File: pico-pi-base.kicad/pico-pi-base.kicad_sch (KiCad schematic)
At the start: 10 parts, among them J1 GPIO, J2 JST-PH2 Bat Ext, J3 Grove, J4 JST-PH2 Bat Int, J5 Conn_SPI1, SW1 SW_Push, U1 Pico_nodbg

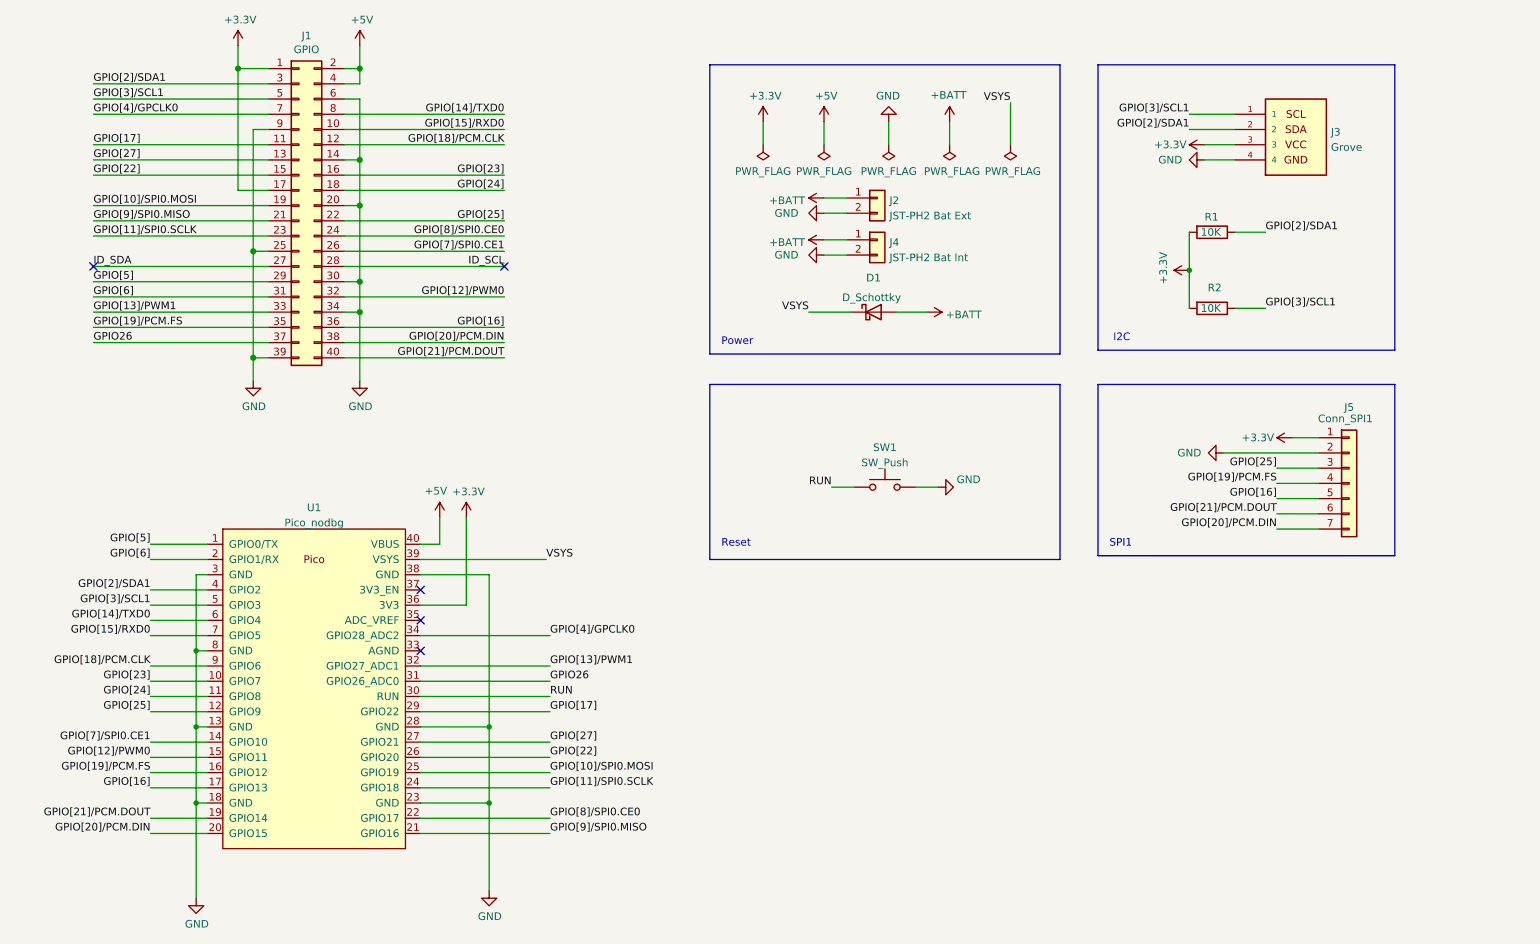
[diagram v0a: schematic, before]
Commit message: pico-pi-base Rev 1.2
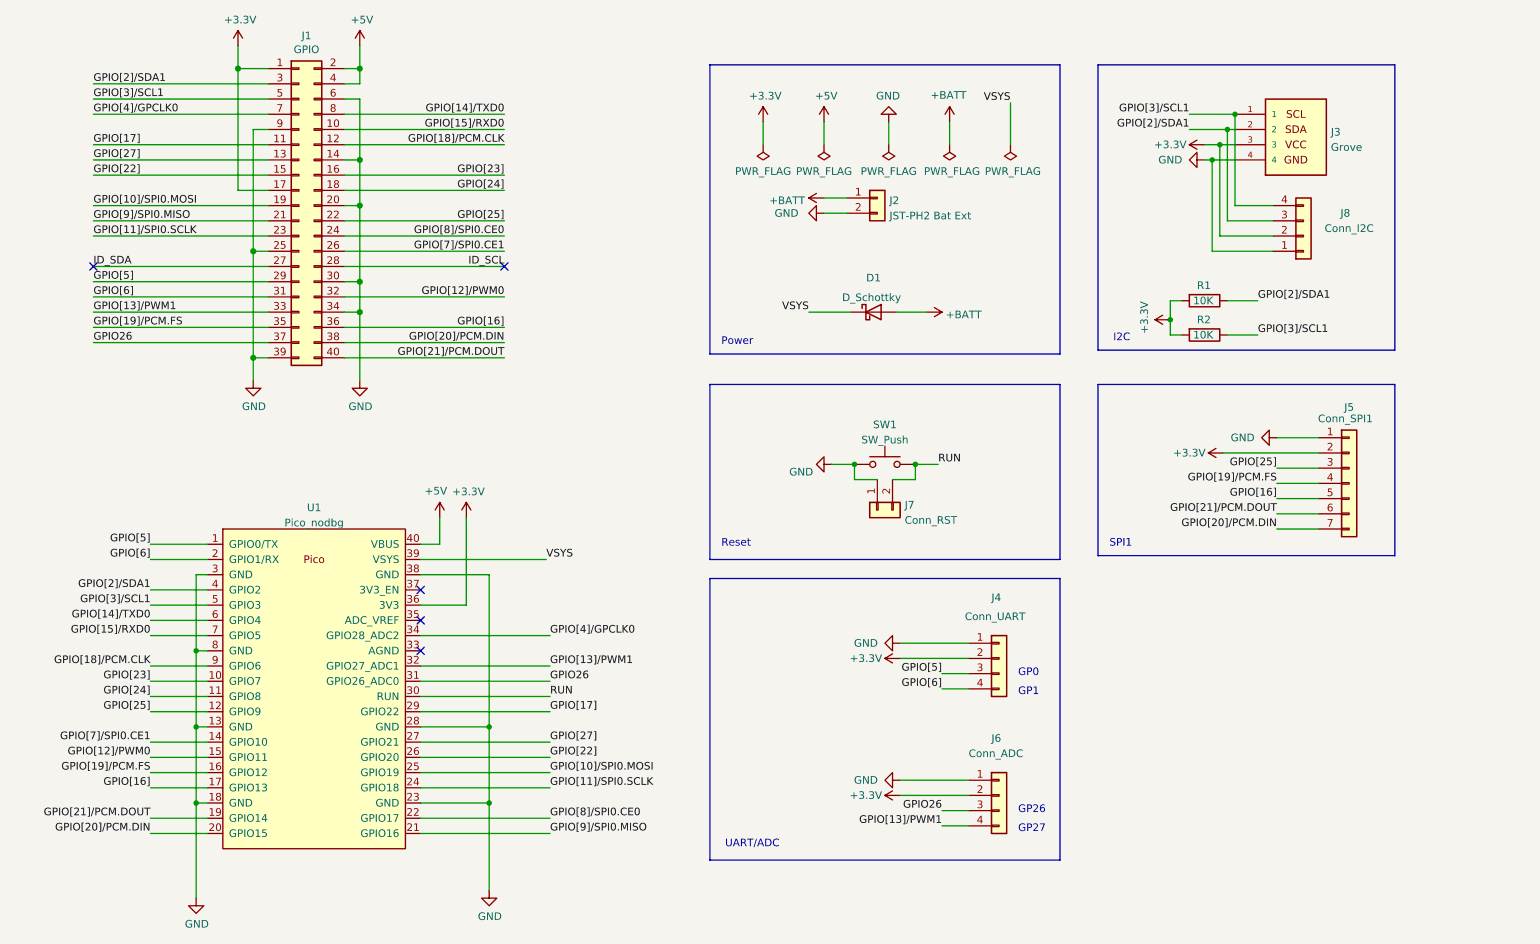
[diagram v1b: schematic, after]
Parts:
- removed J4: JST-PH2 Bat Int, Connector_JST:JST_PH_S2B-PH-SM4-TB_1x02-1MP_P2.00mm_Horizontal, symbol Connector_Generic:Conn_01x02
- added J4: Conn_UART, Connector_PinSocket_2.54mm:PinSocket_1x04_P2.54mm_Horizontal, symbol Connector_Generic:Conn_01x04
- added J6: Conn_ADC, Connector_PinSocket_2.54mm:PinSocket_1x04_P2.54mm_Horizontal, symbol Connector_Generic:Conn_01x04
- added J7: Conn_RST, Connector_PinHeader_2.54mm:PinHeader_1x02_P2.54mm_Horizontal, symbol Connector_Generic:Conn_01x02
- added J8: Conn_I2C, Connector_PinHeader_2.54mm:PinHeader_1x04_P2.54mm_Horizontal, symbol Connector_Generic:Conn_01x04
- J1: footprint Connector_PinSocket_2.54mm:PinSocket_2x20_P2.54mm_Vertical -> Connector_PinHeader_2.54mm:PinHeader_2x20_P2.54mm_Vertical
- R1, R2: LCSC C25744 -> C25804
- SW1: footprint Button_Switch_SMD:SW_SPST_B3U-3000P -> user:Microtaster_Horizontal
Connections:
- net +3.3V: now also J5.2 (Pin_2), J4.2 (Pin_2), J6.2 (Pin_2), J8.2 (Pin_2); no longer J5.1 (Pin_1)
- net GND: now also J5.1 (Pin_1), SW1.1, J4.1 (Pin_1), J6.1 (Pin_1), J7.1 (Pin_1), J8.1 (Pin_1); no longer J5.2 (Pin_2), SW1.2
- net GPIO26: now also J6.3 (Pin_3)
- net GPIO[13]/PWM1: now also J6.4 (Pin_4)
- net GPIO[2]/SDA1: now also J8.3 (Pin_3)
- net GPIO[3]/SCL1: now also J8.4 (Pin_4)
- net GPIO[5]: now also J4.3 (Pin_3)
- net GPIO[6]: now also J4.4 (Pin_4)
- net RUN: now also SW1.2, J7.2 (Pin_2); no longer SW1.1
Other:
- note added: "GP0"
- note added: "GP1"
- note added: "GP26"
- note added: "GP27"
- note added: "UART/ADC"
- moved on the sheet: R1, R2, SW1

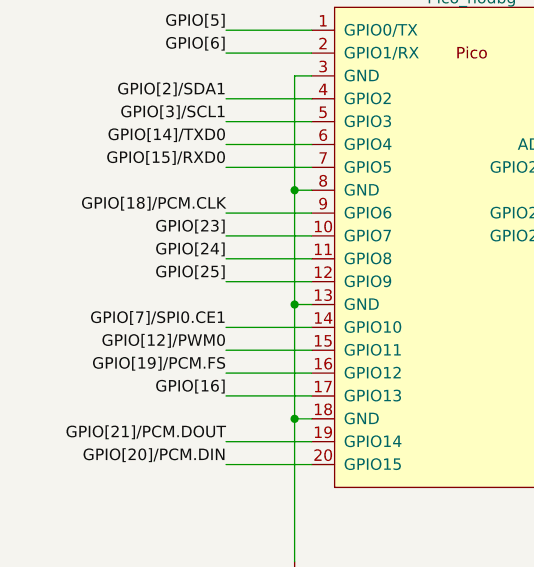
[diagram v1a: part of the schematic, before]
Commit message: Rev 2.0: swapped pins to support I2S
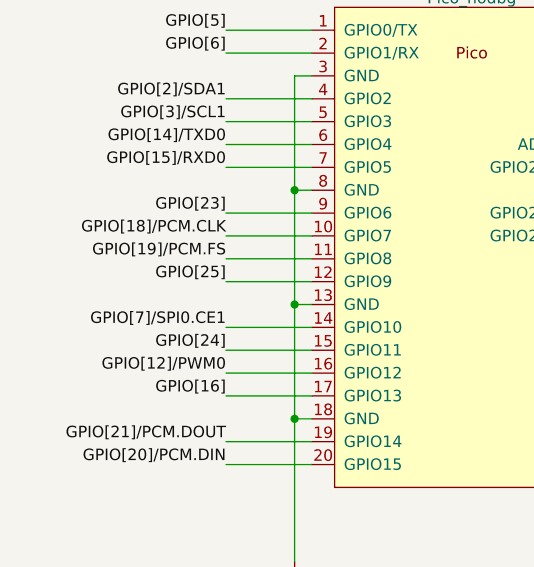
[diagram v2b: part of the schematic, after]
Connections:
- net GPIO[12]/PWM0: now also U1.16 (GPIO12); no longer U1.15 (GPIO11)
- net GPIO[18]/PCM.CLK: now also U1.10 (GPIO7); no longer U1.9 (GPIO6)
- net GPIO[19]/PCM.FS: now also U1.11 (GPIO8); no longer U1.16 (GPIO12)
- net GPIO[23]: now also U1.9 (GPIO6); no longer U1.10 (GPIO7)
- net GPIO[24]: now also U1.15 (GPIO11); no longer U1.11 (GPIO8)
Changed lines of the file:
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@@
   (title_block
     (title "pi-pico-base")
-    (date "2023-04-09")
-    (rev "1.2")
+    (date "2023-04-27")
+    (rev "2.0")
     (company "Bernhard Bablok")
     (comment 1 "https://github.com/bablokb/pcb-pi-pico-base")
@@
     (effects (font (size 1.27 1.27)) (justify left bottom))
   )
-  (label "GPIO[12]{slash}PWM0" (at 41.275 142.875 180)
+  (label "GPIO[12]{slash}PWM0" (at 41.275 145.415 180)
     (effects (font (size 1.27 1.27)) (justify right bottom))
   )
@@
     (effects (font (size 1.27 1.27)) (justify right bottom))
   )
-  (label "GPIO[18]{slash}PCM.CLK" (at 41.275 127.635 180)
+  (label "GPIO[18]{slash}PCM.CLK" (at 41.275 130.175 180)
     (effects (font (size 1.27 1.27)) (justify right bottom))
   )
@@
     (effects (font (size 1.27 1.27)) (justify right bottom))
   )
-  (label "GPIO[23]" (at 41.275 130.175 180)
+  (label "GPIO[23]" (at 41.275 127.635 180)
     (effects (font (size 1.27 1.27)) (justify right bottom))
   )
@@
     (effects (font (size 1.27 1.27)) (justify left bottom))
   )
-  (label "GPIO[24]" (at 41.275 132.715 180)
+  (label "GPIO[24]" (at 41.275 142.875 180)
     (effects (font (size 1.27 1.27)) (justify right bottom))
   )
@@
     (effects (font (size 1.27 1.27)) (justify left bottom))
   )
-  (label "GPIO[19]{slash}PCM.FS" (at 41.275 145.415 180)
-    (effects (font (size 1.27 1.27)) (justify right bottom))
-  )
+  (label "GPIO[19]{slash}PCM.FS" (at 41.275 132.715 180)
+    (effects (font (size 1.27 1.27)) (justify right bottom))
+  )

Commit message: Rev 2.1: add MicroSD-BFF
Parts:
- added JP1: ADC0/SD_CS, Jumper:SolderJumper-3_P1.3mm_Bridged12_Pad1.0x1.5mm, symbol Jumper:SolderJumper_3_Bridged12
- added U2: SD-BFF, user:SD_BFF, symbol user:SD-BFF
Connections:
- net +3.3V: now also U2.5 (3V3)
- net GND: now also U2.6 (GND)
- net GPIO26: now also JP1.2 (C); no longer J6.3 (Pin_3)
- net GPIO[10]/SPI0.MOSI: now also U2.4 (MOSI)
- net GPIO[11]/SPI0.SCLK: now also U2.2 (SCK)
- net GPIO[9]/SPI0.MISO: now also U2.3 (MISO)
- new net ADC0: J6.3 (Pin_3), JP1.3 (B)
- new net SD_CS: JP1.1 (A), U2.14 (TX)
- no-connect marks 5 -> 13
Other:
- note added: "ADC1"
- note added: "SD-BFF"
- note removed: "GP26"
- note removed: "GP27"

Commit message: pico-pi-base: Rev. 2.2
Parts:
- removed U2: SD-BFF, user:SD_BFF, symbol user:SD-BFF
- added J9: Micro_SD_TF_PUSH, user:TF-Push, symbol user:Micro_SD_TF_PUSH
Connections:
- net +3.3V: now also J9.4 (VDD)
- net GND: now also J9.10 (SHIELD), J9.11 (SHIELD), J9.12 (SHIELD), J9.13 (SHIELD), J9.6 (VSS)
- net GPIO[10]/SPI0.MOSI: now also J9.3 (CMD)
- net GPIO[11]/SPI0.SCLK: now also J9.5 (CLK)
- net GPIO[9]/SPI0.MISO: now also J9.7 (DAT0)
- net SD_CS: now also J9.2 (DAT3/CD)
- no-connect marks 13 -> 8
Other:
- note added: "MicroSD-Card-Reader"
- note removed: "SD-BFF"
